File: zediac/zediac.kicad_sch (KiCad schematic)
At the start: 137 parts, among them J1 Conn_02x20_Odd_Even, J2 Conn_01x03_Male, J3 Conn_02x12_Odd_Even, J4 Conn_01x03_Male, J5 Conn_02x05_Odd_Even, J6 Conn_01x03_Male, J7 Screw_Terminal_01x02, J8 Barrel_Jack, P1 USB_C_Plug_USB2.0, Q1 Q_PMOS_GDS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

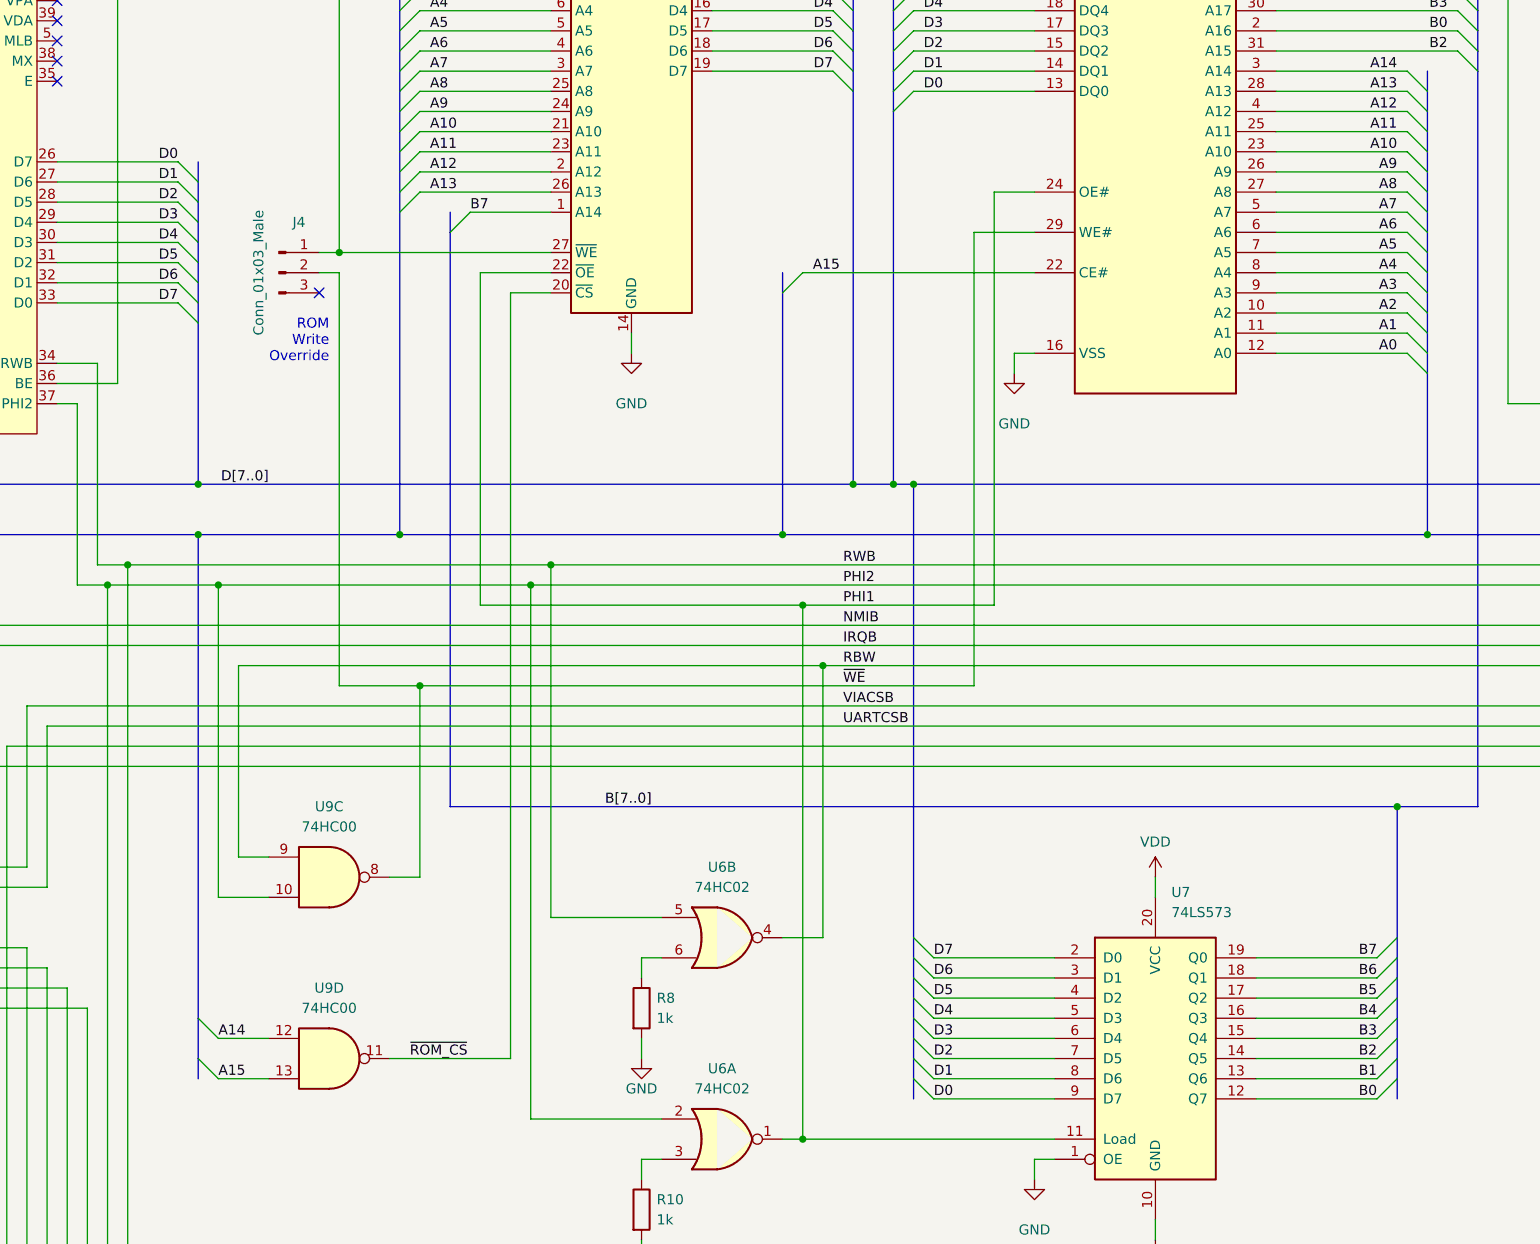
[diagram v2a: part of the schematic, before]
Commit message: Fix reversed databus on '816
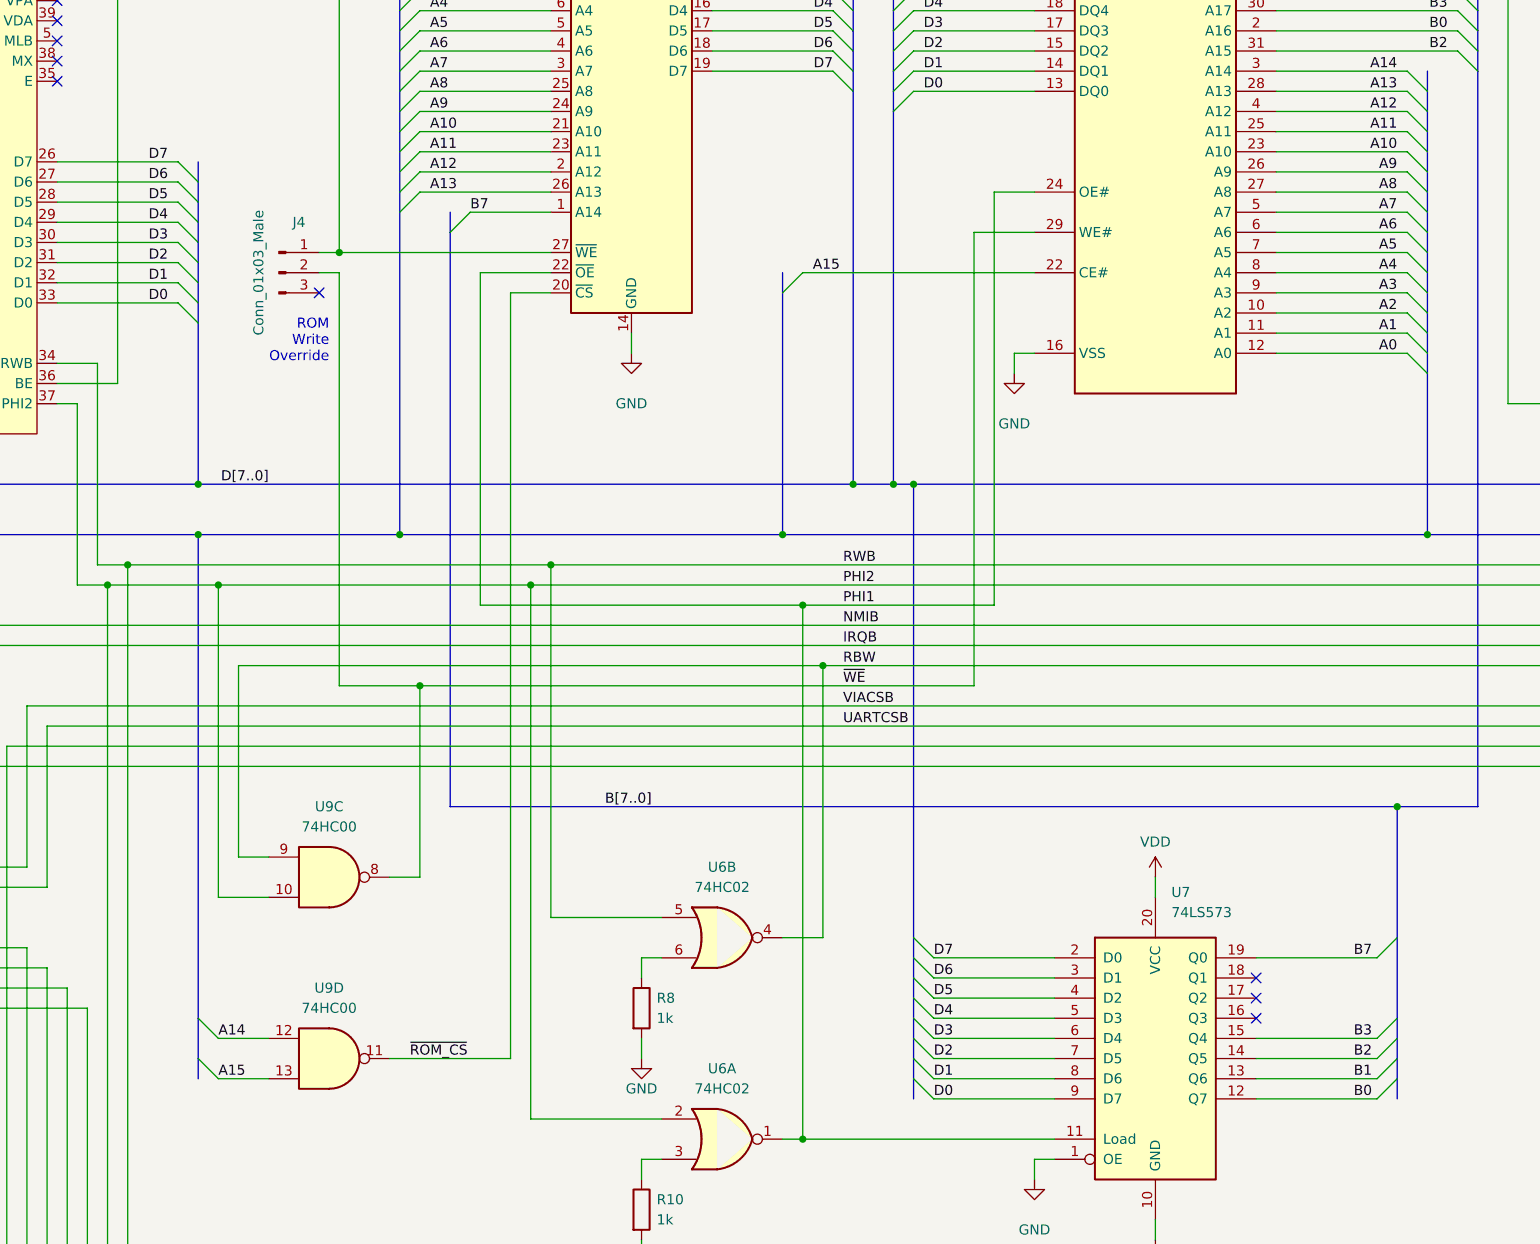
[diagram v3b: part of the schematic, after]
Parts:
- U12: footprint Package_DFN_QFN:VQFN-20-1EP_3x3mm_P0.45mm_EP1.55x1.55mm -> Package_DFN_QFN:SiliconLabs_QFN-20-1EP_3x3mm_P0.5mm_EP1.8x1.8mm
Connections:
- net D0: now also U3.33 (D0); no longer U3.26 (D7)
- net D1: now also U3.32 (D1); no longer U3.27 (D6)
- net D2: now also U3.31 (D2); no longer U3.28 (D5)
- net D3: now also U3.30 (D3); no longer U3.29 (D4)
- net D4: now also U3.29 (D4); no longer U3.30 (D3)
- net D5: now also U3.28 (D5); no longer U3.31 (D2)
- net D6: now also U3.27 (D6); no longer U3.32 (D1)
- net D7: now also U3.26 (D7); no longer U3.33 (D0)
- net B4: no longer names the net of U7.16 (Q3)
- net B5: no longer names the net of U7.17 (Q2)
- net B6: no longer names the net of U7.18 (Q1)
- no-connect marks 21 -> 24
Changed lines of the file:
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@@
   (no_connect (at 91.44 132.08))
   (no_connect (at 548.64 173.99))
+  (no_connect (at 242.57 257.81))
   (no_connect (at 293.37 177.8))
   (no_connect (at 124.46 166.37))
   (no_connect (at 434.34 149.86))
+  (no_connect (at 242.57 252.73))
   (no_connect (at 78.74 243.84))
+  (no_connect (at 242.57 255.27))
   (no_connect (at 472.44 189.23))
   (no_connect (at 434.34 173.99))
@@
     (stroke (width 0) (type default) (color 0 0 0 0))
   )
-  (bus_entry (at 260.35 250.19) (size -2.54 2.54)
-    (stroke (width 0) (type default) (color 0 0 0 0))
-  )
   (bus_entry (at 270.51 138.43) (size -2.54 -2.54)
     (stroke (width 0) (type default) (color 0 0 0 0))
@@
     (stroke (width 0) (type default) (color 0 0 0 0))
   )
-  (bus_entry (at 260.35 255.27) (size -2.54 2.54)
-    (stroke (width 0) (type default) (color 0 0 0 0))
-  )
   (bus_entry (at 134.62 151.13) (size 2.54 -2.54)
     (stroke (width 0) (type default) (color 0 0 0 0))
@@
     (stroke (width 0) (type default) (color 0 0 0 0))
   )
-  (bus_entry (at 260.35 252.73) (size -2.54 2.54)
-    (stroke (width 0) (type default) (color 0 0 0 0))
-  )
   (bus_entry (at 30.48 312.42) (size 2.54 2.54)
     (stroke (width 0) (type default) (color 0 0 0 0))
@@
     (stroke (width 0) (type default) (color 0 0 0 0))
   )
-  (wire (pts (xy 242.57 252.73) (xy 257.81 252.73))
-    (stroke (width 0) (type default) (color 0 0 0 0))
-  )
   (wire (pts (xy 367.03 290.83) (xy 378.46 290.83))
     (stroke (width 0) (type default) (color 0 0 0 0))
@@
     (stroke (width 0) (type default) (color 0 0 0 0))
   )
-  (bus (pts (xy 260.35 250.19) (xy 260.35 247.65))
-    (stroke (width 0) (type default) (color 0 0 0 0))
-  )
   (bus (pts (xy 281.94 250.19) (xy 281.94 252.73))
     (stroke (width 0) (type default) (color 0 0 0 0))
@@
     (stroke (width 0) (type default) (color 0 0 0 0))
   )
-  (bus (pts (xy 260.35 257.81) (xy 260.35 255.27))
-    (stroke (width 0) (type default) (color 0 0 0 0))
-  )
   (wire (pts (xy 48.895 299.72) (xy 48.895 331.47))
     (stroke (width 0) (type default) (color 0 0 0 0))
@@
     (stroke (width 0) (type default) (color 0 0 0 0))
   )
-  (wire (pts (xy 242.57 255.27) (xy 257.81 255.27))
-    (stroke (width 0) (type default) (color 0 0 0 0))
-  )
   (wire (pts (xy 43.815 304.8) (xy 43.815 333.375))
     (stroke (width 0) (type default) (color 0 0 0 0))
@@
     (stroke (width 0) (type default) (color 0 0 0 0))
   )
-  (wire (pts (xy 242.57 257.81) (xy 257.81 257.81))
-    (stroke (width 0) (type default) (color 0 0 0 0))
-  )
   (wire (pts (xy 524.51 189.23) (xy 546.1 189.23))
     (stroke (width 0) (type default) (color 0 0 0 0))
@@
     (stroke (width 0) (type default) (color 0 0 0 0))
   )
-  (bus (pts (xy 260.35 255.27) (xy 260.35 252.73))
-    (stroke (width 0) (type default) (color 0 0 0 0))
-  )
   (wire (pts (xy 510.54 85.09) (xy 510.54 87.63))
     (stroke (width 0) (type default) (color 0 0 0 0))
@@
     (stroke (width 0) (type default) (color 0 0 0 0))
   )
-  (bus (pts (xy 260.35 252.73) (xy 260.35 250.19))
+  (bus (pts (xy 260.35 247.65) (xy 260.35 257.81))
     (stroke (width 0) (type default) (color 0 0 0 0))
   )
@@
     (effects (font (size 1.27 1.27)) (justify right bottom))
   )
-  (label "B5" (at 257.81 255.27 180)
-    (effects (font (size 1.27 1.27)) (justify right bottom))
-  )
   (label "VIACSB" (at 190.5 218.44 0)
     (effects (font (size 1.27 1.27)) (justify left bottom))
@@
     (effects (font (size 1.27 1.27)) (justify right bottom))
   )
-  (label "D1" (at 106.68 152.4 180)
+  (label "D1" (at 105.41 165.1 180)
     (effects (font (size 1.27 1.27)) (justify right bottom))
   )
@@
     (effects (font (size 1.27 1.27)) (justify right bottom))
   )
-  (label "D2" (at 106.68 154.94 180)
+  (label "D2" (at 105.41 162.56 180)
     (effects (font (size 1.27 1.27)) (justify right bottom))
   )
-  (label "B0" (at 257.81 267.97 180)
+  (label "B0" (at 257.175 267.97 180)
     (effects (font (size 1.27 1.27)) (justify right bottom))
   )
@@
     (effects (font (size 1.27 1.27)) (justify left bottom))
   )
-  (label "D5" (at 106.68 162.56 180)
+  (label "D5" (at 105.41 154.94 180)
     (effects (font (size 1.27 1.27)) (justify right bottom))
   )
@@
     (effects (font (size 1.27 1.27)) (justify left bottom))
   )
-  (label "B3" (at 257.81 260.35 180)
+  (label "B3" (at 257.175 260.35 180)
     (effects (font (size 1.27 1.27)) (justify right bottom))
   )
@@
     (effects (font (size 1.27 1.27)) (justify left bottom))
   )
-  (label "B4" (at 257.81 257.81 180)
-    (effects (font (size 1.27 1.27)) (justify right bottom))
-  )
   (label "IO.PB6" (at 285.75 280.67 0)
     (effects (font (size 1.27 1.27)) (justify left bottom))
@@
     (effects (font (size 1.27 1.27)) (justify right bottom))
   )
-  (label "D3" (at 106.68 157.48 180)
+  (label "D3" (at 105.41 160.02 180)
     (effects (font (size 1.27 1.27)) (justify right bottom))
   )
@@
     (effects (font (size 1.27 1.27)) (justify left bottom))
   )
-  (label "D0" (at 106.68 149.86 180)
+  (label "D0" (at 105.41 167.64 180)
     (effects (font (size 1.27 1.27)) (justify right bottom))
   )
@@
     (effects (font (size 1.27 1.27)) (justify right bottom))
   )
-  (label "B2" (at 257.81 262.89 180)
+  (label "B2" (at 257.175 262.89 180)
     (effects (font (size 1.27 1.27)) (justify right bottom))
   )
@@
     (effects (font (size 1.27 1.27)) (justify left bottom))
   )
-  (label "D7" (at 106.68 167.64 180)
+  (label "D7" (at 105.41 149.86 180)
     (effects (font (size 1.27 1.27)) (justify right bottom))
   )
@@
     (effects (font (size 1.27 1.27)) (justify left bottom))
   )
-  (label "B1" (at 257.81 265.43 180)
+  (label "B1" (at 257.175 265.43 180)
     (effects (font (size 1.27 1.27)) (justify right bottom))
   )
@@
     (effects (font (size 1.27 1.27)) (justify left bottom))
   )
-  (label "B7" (at 257.81 250.19 180)
+  (label "B7" (at 257.175 250.19 180)
     (effects (font (size 1.27 1.27)) (justify right bottom))
   )
@@
     (effects (font (size 1.27 1.27)) (justify left bottom))
   )
-  (label "B6" (at 257.81 252.73 180)
-    (effects (font (size 1.27 1.27)) (justify right bottom))
-  )
   (label "A9" (at 138.43 143.51 0)
     (effects (font (size 1.27 1.27)) (justify left bottom))
@@
     (effects (font (size 1.27 1.27)) (justify right bottom))
   )
-  (label "D4" (at 106.68 160.02 180)
+  (label "D4" (at 105.41 157.48 180)
     (effects (font (size 1.27 1.27)) (justify right bottom))
   )
@@
     (effects (font (size 1.27 1.27)) (justify right bottom))
   )
-  (label "D6" (at 106.68 165.1 180)
+  (label "D6" (at 105.41 152.4 180)
     (effects (font (size 1.27 1.27)) (justify right bottom))
   )
@@
       (effects (font (size 1.27 1.27)) (justify right))
     )
-    (property "Footprint" "Package_DFN_QFN:VQFN-20-1EP_3x3mm_P0.45mm_EP1.55x1.55mm" (id 2) (at 453.39 213.36 0)
+    (property "Footprint" "Package_DFN_QFN:SiliconLabs_QFN-20-1EP_3x3mm_P0.5mm_EP1.8x1.8mm" (id 2) (at 453.39 213.36 0)
       (effects (font (size 1.27 1.27)) hide)
     )
@@
     )
     (path "/ac034c2c-d0fc-40bf-841f-8a3faf6a0db7"
-      (reference "U12") (unit 1) (value "CP2102N-Axx-xQFN20") (footprint "Package_DFN_QFN:VQFN-20-1EP_3x3mm_P0.45mm_EP1.55x1.55mm")
+      (reference "U12") (unit 1) (value "CP2102N-Axx-xQFN20") (footprint "Package_DFN_QFN:SiliconLabs_QFN-20-1EP_3x3mm_P0.5mm_EP1.8x1.8mm")
     )
     (path "/816b4d43-b0d3-4703-ad45-48368d06b2a7"
